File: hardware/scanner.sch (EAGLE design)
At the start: 24 parts, among them K1 PIN20X2, U1 CAT24C32WI-GT3, U2 TPS61165DBV

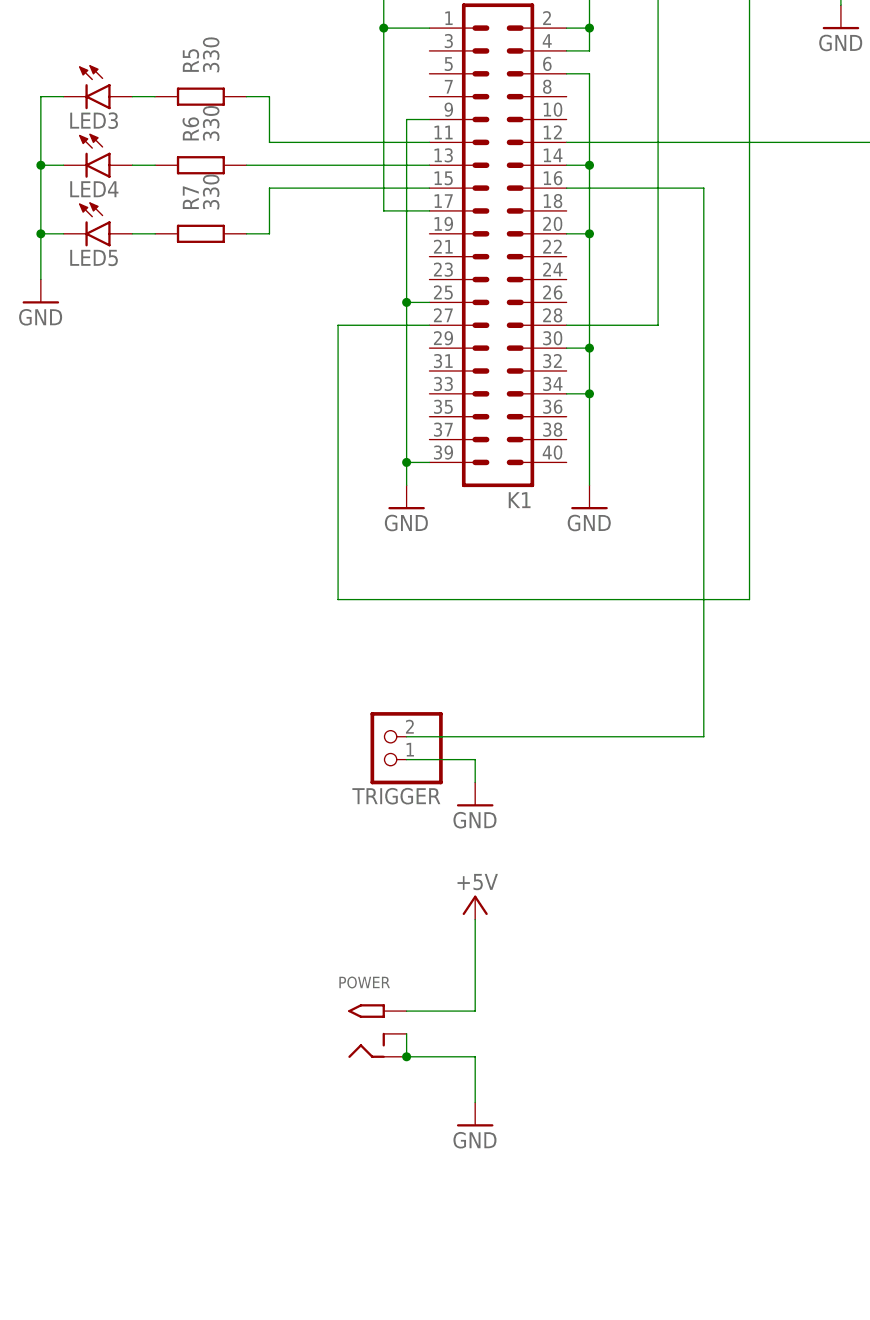
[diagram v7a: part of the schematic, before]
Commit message: added proper sensor connector
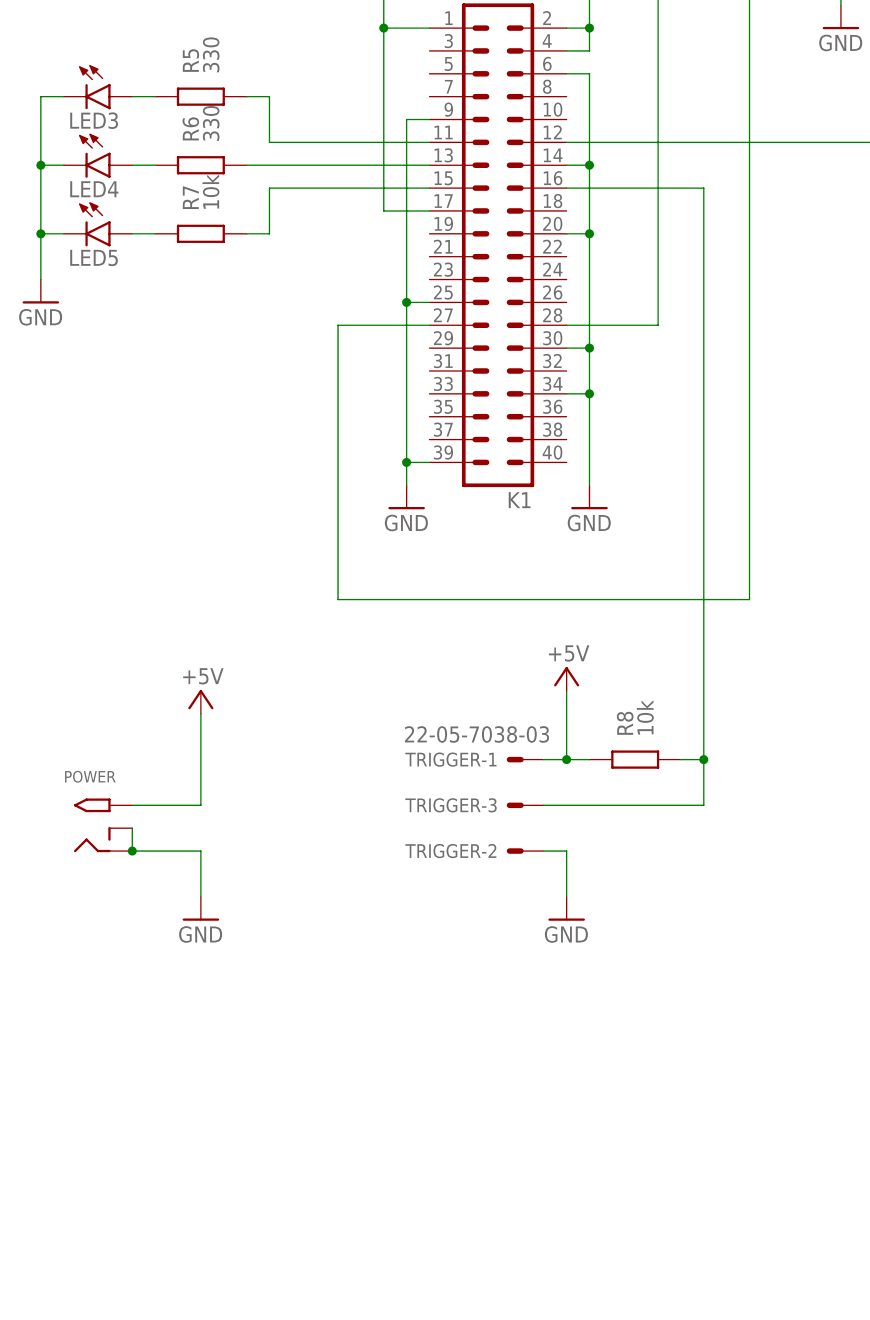
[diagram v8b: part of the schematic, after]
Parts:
- added R8: 10k, resistor:R-EU_M0805
- R7: value 330 -> 10k
- TRIGGER: value (none) -> 22-05-7038-03; device pinhead:PINHD-1X2 -> con-molex:22-05-7038-03
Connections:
- net +5V: now also R8.2, TRIGGER-1.S
- net GND: now also TRIGGER-2.S; no longer TRIGGER.1
- net TRIGGER: now also R8.1, TRIGGER-3.S; no longer TRIGGER.2
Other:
- moved on the sheet: POWER
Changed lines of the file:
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@@
 </part>
 <part name="+3V2" library="supply1" deviceset="+3V3" device=""/>
-<part name="TRIGGER" library="pinhead" library_urn="urn:adsk.eagle:library:325" deviceset="PINHD-1X2" device="" package3d_urn="urn:adsk.eagle:package:22435/2"/>
 <part name="JP1" library="pinhead" library_urn="urn:adsk.eagle:library:325" deviceset="PINHD-1X2" device="" package3d_urn="urn:adsk.eagle:package:22435/2"/>
 <part name="GND6" library="supply1" deviceset="GND" device=""/>
@@
 </part>
 <part name="LED5" library="led" library_urn="urn:adsk.eagle:library:259" deviceset="LED" device="CHIP-LED0805" package3d_urn="urn:adsk.eagle:package:15818/2"/>
-<part name="R7" library="resistor" deviceset="R-EU_" device="M0805" value="330">
+<part name="R7" library="resistor" deviceset="R-EU_" device="M0805" value="10k">
 <attribute name="TOLERANCE" value="5%"/>
 </part>
 <part name="POWER" library="adafruit" library_urn="urn:adsk.eagle:library:420" deviceset="2.1MMJACK" device="THM" package3d_urn="urn:adsk.eagle:package:6240341/1"/>
+<part name="TRIGGER" library="con-molex" library_urn="urn:adsk.eagle:library:165" deviceset="22-?-03" device="05-7038"/>
+<part name="P+4" library="supply1" deviceset="+5V" device=""/>
+<part name="R8" library="resistor" deviceset="R-EU_" device="M0805" value="10k">
+<attribute name="TOLERANCE" value="5%"/>
+</part>
 </parts>
 <sheets>
@@
 <attribute name="VALUE" x="144.78" y="168.148" size="1.778" layer="96"/>
 </instance>
-<instance part="GND4" gate="1" x="81.28" y="88.9" smashed="yes">
-<attribute name="VALUE" x="78.74" y="86.36" size="1.778" layer="96"/>
+<instance part="GND4" gate="1" x="91.44" y="76.2" smashed="yes">
+<attribute name="VALUE" x="88.9" y="73.66" size="1.778" layer="96"/>
 </instance>
 <instance part="P+2" gate="1" x="132.08" y="198.12" smashed="yes">
@@
 <attribute name="VALUE" x="129.54" y="243.84" size="1.778" layer="96" rot="R180"/>
 </instance>
-<instance part="TRIGGER" gate="G$1" x="71.12" y="96.52" smashed="yes" rot="R180">
-<attribute name="NAME" x="77.47" y="90.805" size="1.778" layer="95" rot="R180"/>
-<attribute name="VALUE" x="77.47" y="101.6" size="1.778" layer="96" rot="R180"/>
-</instance>
 <instance part="JP1" gate="G$1" x="73.66" y="203.2" smashed="yes" rot="R270">
 <attribute name="NAME" x="79.375" y="209.55" size="1.778" layer="95" rot="R270"/>
 <attribute name="VALUE" x="68.58" y="209.55" size="1.778" layer="96" rot="R270"/>
 </instance>
-<instance part="GND6" gate="1" x="81.28" y="53.34" smashed="yes">
-<attribute name="VALUE" x="78.74" y="50.8" size="1.778" layer="96"/>
-</instance>
-<instance part="P+3" gate="1" x="81.28" y="78.74" smashed="yes">
-<attribute name="VALUE" x="83.82" y="81.28" size="1.778" layer="96" rot="R180"/>
+<instance part="GND6" gate="1" x="50.8" y="76.2" smashed="yes">
+<attribute name="VALUE" x="48.26" y="73.66" size="1.778" layer="96"/>
+</instance>
+<instance part="P+3" gate="1" x="50.8" y="101.6" smashed="yes">
+<attribute name="VALUE" x="53.34" y="104.14" size="1.778" layer="96" rot="R180"/>
 </instance>
 <instance part="C2" gate="G$1" x="160.02" y="154.94" smashed="yes">
@@
 <attribute name="VALUE" x="52.832" y="154.94" size="1.778" layer="96" rot="R90"/>
 </instance>
-<instance part="POWER" gate="G$1" x="68.58" y="63.5" smashed="yes">
-<attribute name="NAME" x="66.04" y="68.58" size="1.27" layer="95"/>
+<instance part="POWER" gate="G$1" x="38.1" y="86.36" smashed="yes">
+<attribute name="NAME" x="35.56" y="91.44" size="1.27" layer="95"/>
+</instance>
+<instance part="TRIGGER" gate="-1" x="86.36" y="93.98" smashed="yes" rot="R180">
+<attribute name="NAME" x="83.82" y="94.742" size="1.524" layer="95" rot="R180"/>
+<attribute name="VALUE" x="89.662" y="97.663" size="1.778" layer="96" rot="R180"/>
+</instance>
+<instance part="TRIGGER" gate="-2" x="86.36" y="83.82" smashed="yes" rot="R180">
+<attribute name="NAME" x="83.82" y="84.582" size="1.524" layer="95" rot="R180"/>
+</instance>
+<instance part="TRIGGER" gate="-3" x="86.36" y="88.9" smashed="yes" rot="R180">
+<attribute name="NAME" x="83.82" y="89.662" size="1.524" layer="95" rot="R180"/>
+</instance>
+<instance part="P+4" gate="1" x="91.44" y="104.14" smashed="yes">
+<attribute name="VALUE" x="93.98" y="106.68" size="1.778" layer="96" rot="R180"/>
+</instance>
+<instance part="R8" gate="G$1" x="99.06" y="93.98" smashed="yes" rot="R180">
+<attribute name="TOLERANCE" x="99.06" y="93.98" size="1.778" layer="96" rot="R180" display="off"/>
+<attribute name="NAME" x="98.8314" y="96.52" size="1.778" layer="95" rot="R90"/>
+<attribute name="VALUE" x="101.092" y="96.52" size="1.778" layer="96" rot="R90"/>
 </instance>
 </instances>
@@
 <junction x="93.98" y="139.7"/>
 <junction x="93.98" y="134.62"/>
-</segment>
-<segment>
-<wire x1="73.66" y1="93.98" x2="81.28" y2="93.98" width="0.1524" layer="91"/>
-<pinref part="GND4" gate="1" pin="GND"/>
-<wire x1="81.28" y1="93.98" x2="81.28" y2="91.44" width="0.1524" layer="91"/>
-<pinref part="TRIGGER" gate="G$1" pin="1"/>
 </segment>
 <segment>
@@
 </segment>
 <segment>
-<wire x1="81.28" y1="60.96" x2="81.28" y2="55.88" width="0.1524" layer="91"/>
+<wire x1="50.8" y1="83.82" x2="50.8" y2="78.74" width="0.1524" layer="91"/>
 <pinref part="GND6" gate="1" pin="GND"/>
 <pinref part="POWER" gate="G$1" pin="RING_SW"/>
 <pinref part="POWER" gate="G$1" pin="RING"/>
-<wire x1="73.66" y1="63.5" x2="73.66" y2="60.96" width="0.1524" layer="91"/>
-<wire x1="73.66" y1="60.96" x2="81.28" y2="60.96" width="0.1524" layer="91"/>
-<junction x="73.66" y="60.96"/>
+<wire x1="43.18" y1="86.36" x2="43.18" y2="83.82" width="0.1524" layer="91"/>
+<wire x1="43.18" y1="83.82" x2="50.8" y2="83.82" width="0.1524" layer="91"/>
+<junction x="43.18" y="83.82"/>
 </segment>
 <segment>
@@
 <wire x1="35.56" y1="152.4" x2="33.02" y2="152.4" width="0.1524" layer="91"/>
 <junction x="33.02" y="152.4"/>
+</segment>
+<segment>
+<pinref part="TRIGGER" gate="-2" pin="S"/>
+<wire x1="88.9" y1="83.82" x2="91.44" y2="83.82" width="0.1524" layer="91"/>
+<wire x1="91.44" y1="83.82" x2="91.44" y2="78.74" width="0.1524" layer="91"/>
+<pinref part="GND4" gate="1" pin="GND"/>
 </segment>
 </net>
@@
 <segment>
 <pinref part="P+3" gate="1" pin="+5V"/>
-<wire x1="73.66" y1="66.04" x2="81.28" y2="66.04" width="0.1524" layer="91"/>
-<wire x1="81.28" y1="66.04" x2="81.28" y2="76.2" width="0.1524" layer="91"/>
+<wire x1="43.18" y1="88.9" x2="50.8" y2="88.9" width="0.1524" layer="91"/>
+<wire x1="50.8" y1="88.9" x2="50.8" y2="99.06" width="0.1524" layer="91"/>
 <pinref part="POWER" gate="G$1" pin="TIP"/>
+</segment>
+<segment>
+<pinref part="TRIGGER" gate="-1" pin="S"/>
+<wire x1="88.9" y1="93.98" x2="91.44" y2="93.98" width="0.1524" layer="91"/>
+<wire x1="91.44" y1="93.98" x2="91.44" y2="101.6" width="0.1524" layer="91"/>
+<pinref part="P+4" gate="1" pin="+5V"/>
+<pinref part="R8" gate="G$1" pin="2"/>
+<wire x1="91.44" y1="93.98" x2="93.98" y2="93.98" width="0.1524" layer="91"/>
+<junction x="91.44" y="93.98"/>
 </segment>
 </net>
 <net name="TRIGGER" class="0">
 <segment>
-<wire x1="73.66" y1="96.52" x2="106.68" y2="96.52" width="0.1524" layer="91"/>
-<wire x1="106.68" y1="96.52" x2="106.68" y2="157.48" width="0.1524" layer="91"/>
+<wire x1="88.9" y1="88.9" x2="106.68" y2="88.9" width="0.1524" layer="91"/>
+<wire x1="106.68" y1="88.9" x2="106.68" y2="93.98" width="0.1524" layer="91"/>
 <pinref part="K1" gate="G$1" pin="16"/>
+<wire x1="106.68" y1="93.98" x2="106.68" y2="157.48" width="0.1524" layer="91"/>
 <wire x1="106.68" y1="157.48" x2="91.44" y2="157.48" width="0.1524" layer="91"/>
-<pinref part="TRIGGER" gate="G$1" pin="2"/>
+<pinref part="TRIGGER" gate="-3" pin="S"/>
+<pinref part="R8" gate="G$1" pin="1"/>
+<wire x1="104.14" y1="93.98" x2="106.68" y2="93.98" width="0.1524" layer="91"/>
+<junction x="106.68" y="93.98"/>
 </segment>
 </net>
